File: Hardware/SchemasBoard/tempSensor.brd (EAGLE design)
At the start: 17.5 x 17.8 mm, 9 parts, among them IC1 DS1820

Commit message: a
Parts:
- added R1: 4K7, resistor:R1206W
- moved C1 0.57 mm to (12.6, 12.3)
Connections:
- net N$25: now also R1.1
- net VDD: now also R1.2
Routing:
- net GND: track 13.3 -> 43.2 mm, vias 1 -> 2
- net N$25: track 9.56 -> 20.4 mm
- net VDD: track 29.6 -> 39.5 mm, vias 0 -> 1
- net N$3: track 14.1 -> 12.8 mm

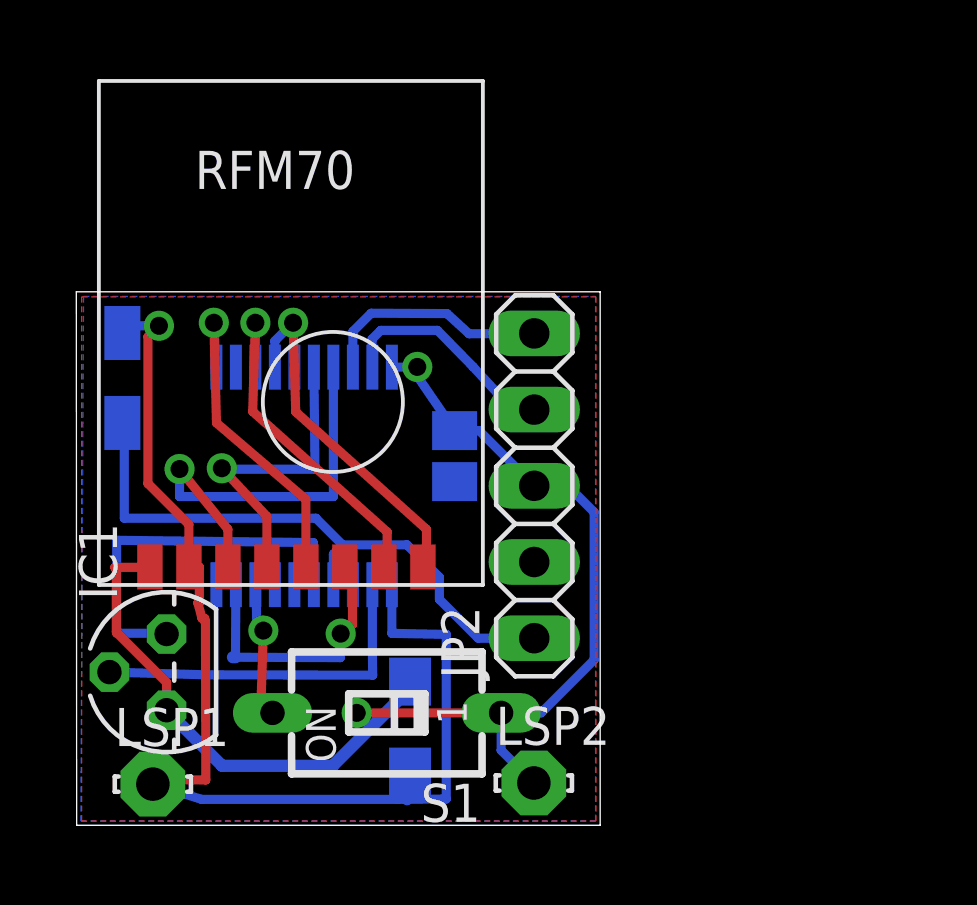
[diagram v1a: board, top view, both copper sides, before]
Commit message: added support for remote IR detector
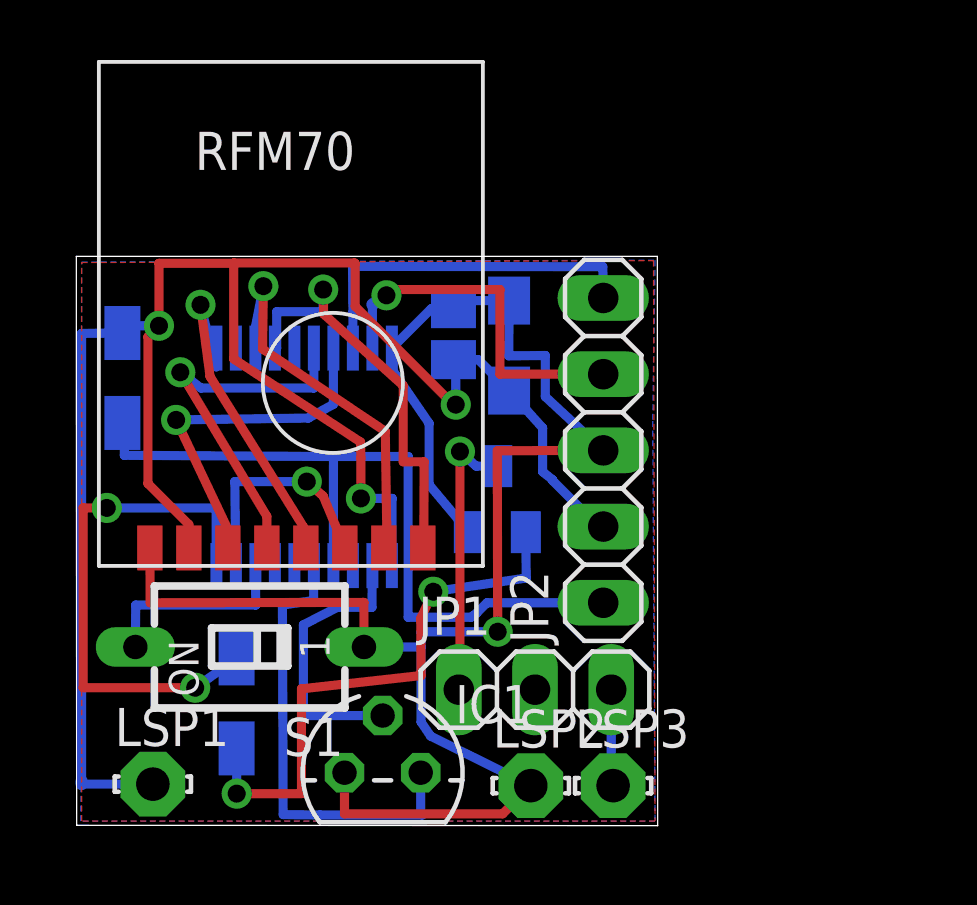
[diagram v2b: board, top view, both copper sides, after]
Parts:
- added JP1: (no value), pinhead:1X03
- added LSP3: LSP11, solpad:LSP11
- added R2: 1K, resistor:R1206W
- added T1: BC846, transistor:SOT23
- moved C2 13.1 mm to (14.4, 16.0)
- moved IC1 7.94 mm to (10.2, 1.75), turned to 0 degrees
- moved S1 5.07 mm to (5.77, 5.94)
- moved C1 4.06 mm to (12.6, 16.4)
- moved JP2 2.58 mm to (17.6, 12.5)
- moved U$1 0.64 mm to (2.54, 23.5)
- moved U$2 0.64 mm to (7.58, 12.3)
- moved LSP2 0.14 mm to (15.1, 1.32)
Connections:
- new net N$4: U$2.12
- new net N$5: JP1.3, LSP3.MP
- new net N$6: R2.2, U$2.10
- new net N$7: R2.1, T1.1
- new net N$9: JP1.1, T1.3
- net GND: now also T1.2
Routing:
- net VDD: track 39.5 -> 66.1 mm, vias 1 -> 3
- net N$7: track 0.00 -> 18.7 mm, vias 0 -> 2
- net N$6: track 0.00 -> 17.8 mm, vias 0 -> 2
- net GND: track 43.2 -> 58.4 mm, vias 2 -> 1
- net N$9: track 0.00 -> 9.39 mm, vias 0 -> 1
- net N$25: track 20.4 -> 26.3 mm
- net N$18: track 7.61 -> 12.3 mm, vias 0 -> 1
- net N$19: track 7.75 -> 12.1 mm
- net N$5: track 0.00 -> 3.26 mm
- net N$3: track 12.8 -> 15.3 mm
- net N$1: track 11.8 -> 9.47 mm
- net N$16: track 14.2 -> 11.9 mm
- net N$20: track 10.4 -> 12.6 mm
- net N$21: track 11.9 -> 14.1 mm
- net N$12: track 11.7 -> 13.8 mm
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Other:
- board size 17.5 x 17.8 mm -> 19.4 x 19 mm

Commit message: a
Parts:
- C1: value (none) -> 100nF
- C2: value (none) -> 1uF
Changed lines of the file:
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@@
 <element name="LSP1" library="solpad" package="LSP11" value="LSP11" x="2.54" y="1.3716"/>
 <element name="LSP2" library="solpad" package="LSP11" value="LSP11" x="15.1384" y="1.3208"/>
-<element name="C1" library="resistor" package="C2012" value="" x="12.5603" y="16.3703" rot="MR90"/>
+<element name="C1" library="resistor" package="C2012" value="100nF" x="12.5603" y="16.3703" rot="MR90"/>
 <element name="S1" library="switch-dil" package="SD4-01" value="" x="5.7658" y="5.9436" rot="R90">
 <attribute name="OC_NEWARK" value="unknown" x="5.7658" y="5.9436" size="1.778" layer="27" rot="R90" display="off"/>
@@
 <attribute name="OC_FARNELL" value="unknown" x="5.7658" y="5.9436" size="1.778" layer="27" rot="R90" display="off"/>
 </element>
-<element name="C2" library="resistor" package="SMC_A" value="" x="14.4145" y="15.9893" rot="MR90"/>
+<element name="C2" library="resistor" package="SMC_A" value="1uF" x="14.4145" y="15.9893" rot="MR90"/>
 <element name="R1" library="resistor" package="R1206W" value="4K7" x="1.524" y="14.9098" rot="MR90"/>
 <element name="JP1" library="pinhead" package="1X03" value="" x="15.2781" y="4.5212"/>

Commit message: aaa
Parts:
- removed JP2: Prog, pinhead:1X05
- added R3: 1K, resistor:R1206W
- added T2: BC846, transistor:SOT23
- added U$3: PROGRAMMINGHEADERDIP, rfm70:PROGHEADER
- LSP1, LSP2, LSP3: value LSP11 -> SE14; device solpad:LSP11 -> solpad:SE14
- S1: value (none) -> DTS-3; device switch-dil:SD4-01 -> switch-tact:DTS-3
- moved R1 22.7 mm to (23.1, 7.77), turned to 0 degrees
- moved LSP1 18.3 mm to (20.9, 1.60)
- moved IC1 16.4 mm to (23.5, 11.5), turned to 180 degrees
- moved R2 11.1 mm to (16.1, 1.50), turned to 0 degrees
- moved LSP2 10.0 mm to (5.09, 1.61), flipped to the bottom
- moved C1 9.55 mm to (19.5, 9.79), turned to 180 degrees
- moved C2 8.95 mm to (17.9, 7.76), turned to 0 degrees
- moved U$1 7.20 mm to (7.21, 18.1)
- moved JP1 7.01 mm to (22.3, 5.21)
- moved T1 6.79 mm to (17.0, 4.79), turned to 180 degrees
- moved LSP3 6.63 mm to (24.5, 1.66)
- moved U$2 5.06 mm to (10.8, 8.41), turned to 270 degrees
- moved S1 3.92 mm to (1.84, 6.01), flipped to the bottom, turned to 270 degrees
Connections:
- removed net N$18: JP2.4, U$2.19
- removed net N$19: JP2.5, U$2.18
- new net N$10: U$3.GND
- new net N$11: U$2.18, U$3.PGC
- new net N$13: T2.3, U$1.GND
- new net N$14: R3.2, T2.1
- new net N$15: R3.1, U$2.15
- new net N$8: U$2.19, U$3.PGD
- net GND: now also T2.2; no longer JP2.3, U$1.GND
- net N$2: now also U$2.3; no longer U$2.8
- net N$25: now also U$3.MCLR; no longer JP2.1
- net N$4: now also JP1.2
- net VDD: now also U$3.VDD; no longer JP2.2
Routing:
- net VDD: track 66.1 -> 24.1 mm, vias 3 -> 0
- net N$14: track 0.00 -> 38.4 mm, vias 0 -> 2
- net N$15: track 0.00 -> 32.1 mm, vias 0 -> 2
- net N$4: track 0.00 -> 31.0 mm
- net N$2: track 6.71 -> 25.7 mm, vias 0 -> 1
- net N$25: track 26.3 -> 40.8 mm, vias 0 -> 3
- net N$7: track 18.7 -> 5.51 mm, vias 2 -> 0
- net N$6: track 17.8 -> 4.98 mm, vias 2 -> 0
- net N$18: track 12.3 -> 0.00 mm, vias 1 -> 0
- net N$19: track 12.1 -> 0.00 mm
- net N$1: track 9.47 -> 17.3 mm, vias 0 -> 1
- net N$11: track 0.00 -> 7.21 mm
- net N$3: track 15.3 -> 9.75 mm, vias 0 -> 1
- net N$13: track 0.00 -> 5.01 mm, vias 0 -> 1
- net N$23: track 8.44 -> 4.03 mm
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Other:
- board size 19.4 x 19 mm -> 26.2 x 13.4 mm
